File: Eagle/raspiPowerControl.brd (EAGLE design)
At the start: 100 x 80 mm, 10 parts, among them Q1 FDN360P, T1 BC847

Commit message: Update Eagle
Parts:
- added C3: 100n, rcl:C0805
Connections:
- net +5V: now also C3.2
- net GND: now also C3.1
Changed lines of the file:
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@@
 <attribute name="VALUE" x="-52.07" y="-50.8" size="1.27" layer="27"/>
+</element>
+<element name="C3" library="rcl" library_urn="urn:adsk.eagle:library:334" package="C0805" package3d_urn="urn:adsk.eagle:package:23617/2" value="100n" x="-57.15" y="-60.96" smashed="yes">
+<attribute name="NAME" x="-58.42" y="-59.69" size="1.27" layer="25"/>
+<attribute name="POPULARITY" value="88" x="-57.15" y="-60.96" size="1.778" layer="27" display="off"/>
+<attribute name="SPICEPREFIX" value="C" x="-57.15" y="-60.96" size="1.778" layer="27" display="off"/>
+<attribute name="VALUE" x="-58.42" y="-63.5" size="1.27" layer="27"/>
 </element>
 </elements>
@@
 <contactref element="SV1" pad="14"/>
 <contactref element="SV1" pad="9"/>
+<contactref element="C3" pad="1"/>
+<wire x1="-51.75" y1="-48.26" x2="-58.1" y2="-60.96" width="0" layer="19" extent="1-1"/>
 <wire x1="-50.8" y1="-38.1" x2="-51.75" y2="-48.26" width="0" layer="19" extent="1-1"/>
 <wire x1="-48.58" y1="-4.91" x2="-50.8" y2="-38.1" width="0" layer="19" extent="1-1"/>
-<wire x1="26.67" y1="26.67" x2="-48.58" y2="-4.91" width="0" layer="19" extent="1-1"/>
-<wire x1="38.1" y1="3.81" x2="26.67" y2="26.67" width="0" layer="19" extent="1-1"/>
+<wire x1="27.94" y1="3.81" x2="-48.58" y2="-4.91" width="0" layer="19" extent="1-1"/>
+<wire x1="33.02" y1="6.35" x2="27.94" y2="3.81" width="0" layer="19" extent="1-1"/>
 <wire x1="38.1" y1="3.81" x2="33.02" y2="6.35" width="0" layer="19" extent="1-1"/>
-<wire x1="27.94" y1="3.81" x2="33.02" y2="6.35" width="0" layer="19" extent="1-1"/>
+<wire x1="26.67" y1="26.67" x2="33.02" y2="6.35" width="0" layer="19" extent="1-1"/>
 </signal>
 <signal name="RP5V">
@@
 <contactref element="Q1" pad="2"/>
 <contactref element="+5V" pad="MP"/>
+<contactref element="C3" pad="2"/>
 <contactref element="LED1" pad="A"/>
+<wire x1="-50.952" y1="-43.18" x2="-56.2" y2="-60.96" width="0" layer="19" extent="1-1"/>
 <wire x1="-50.8" y1="-31.75" x2="-50.952" y2="-43.18" width="0" layer="19" extent="1-1"/>
 <wire x1="-49.85" y1="-24.13" x2="-50.8" y2="-31.75" width="0" layer="19" extent="1-1"/>
@@
 </signal>
 <signal name="PWR">
-<contactref element="LED1" pad="C"/>
 <contactref element="U$1" pad="5V"/>
 <contactref element="C1" pad="2"/>
+<contactref element="LED1" pad="C"/>
 <wire x1="-48.108" y1="-43.18" x2="-49.85" y2="-48.26" width="0" layer="19" extent="1-1"/>
 <wire x1="26.67" y1="29.21" x2="-48.108" y2="-43.18" width="0" layer="19" extent="1-1"/>

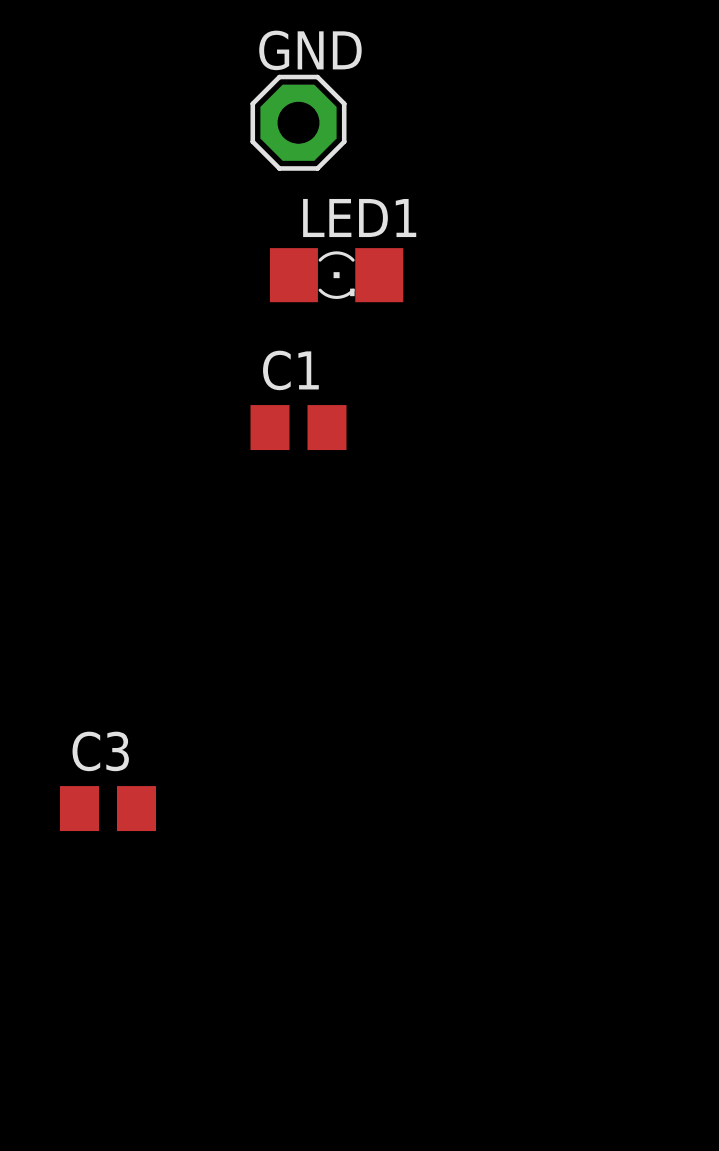
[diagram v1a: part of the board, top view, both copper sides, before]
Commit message: Add regulator to design
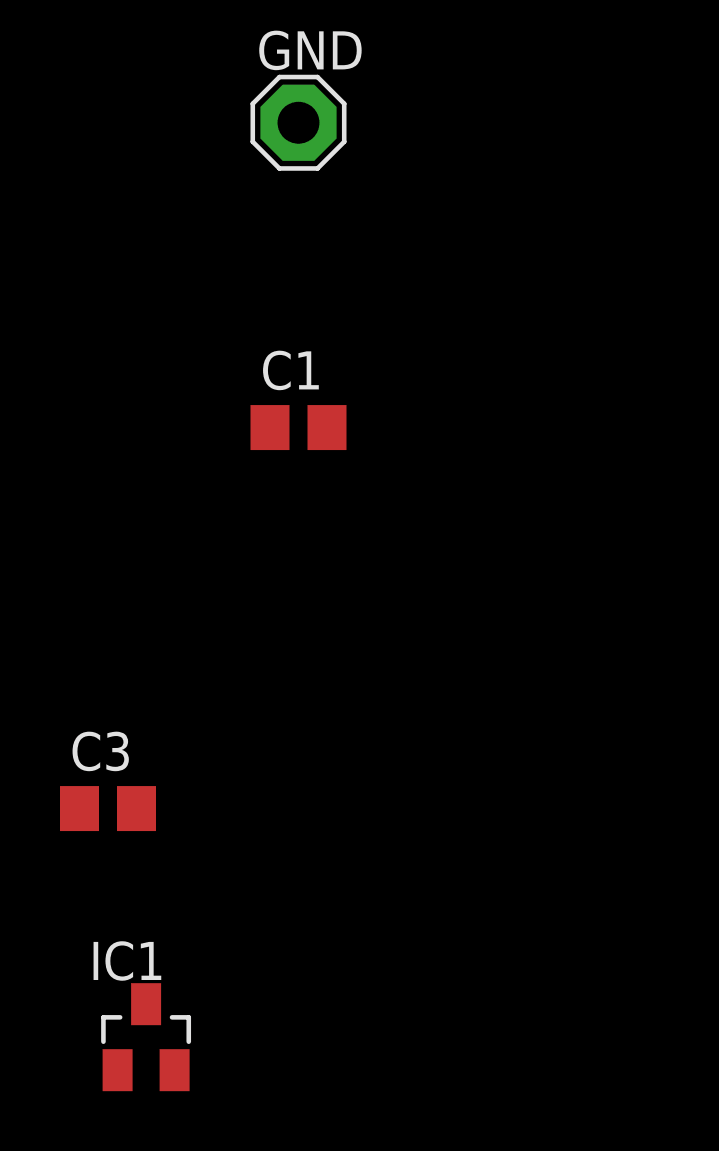
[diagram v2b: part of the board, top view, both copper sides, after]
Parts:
- removed LED1: red (1.7V), led:1206
- added IC1: MCP1702 3.3, linear:SOT23
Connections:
- removed net +5V: +5V.MP, C3.2, LED1.A, Q1.2, R2.2
- new net N$2: +5V.MP, C3.2, IC1.3, Q1.2, R2.2
- net GND: now also IC1.1
- net PWR: now also IC1.2; no longer LED1.C
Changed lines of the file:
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@@
 <attribute name="VALUE" x="-50.8" y="-37.719" size="0.0254" layer="27"/>
-</element>
-<element name="LED1" library="led" library_urn="urn:adsk.eagle:library:259" package="1206" package3d_urn="urn:adsk.eagle:package:15796/2" value="red (1.7V)" x="-49.53" y="-43.18" smashed="yes">
-<attribute name="NAME" x="-50.8" y="-41.91" size="1.27" layer="25"/>
-<attribute name="POPULARITY" value="20" x="-49.53" y="-43.18" size="1.778" layer="27" display="off"/>
-<attribute name="VALUE" x="-50.8" y="-45.72" size="1.27" layer="27"/>
 </element>
 <element name="C1" library="rcl" library_urn="urn:adsk.eagle:library:334" package="C0805" package3d_urn="urn:adsk.eagle:package:23617/2" value="1u" x="-50.8" y="-48.26" smashed="yes">
@@
 <attribute name="SPICEPREFIX" value="C" x="-57.15" y="-60.96" size="1.778" layer="27" display="off"/>
 <attribute name="VALUE" x="-58.42" y="-63.5" size="1.27" layer="27"/>
+</element>
+<element name="IC1" library="linear" library_urn="urn:adsk.eagle:library:262" package="SOT23" package3d_urn="urn:adsk.eagle:package:16489/2" value="MCP1702 3.3" x="-55.88" y="-68.58" smashed="yes">
+<attribute name="NAME" x="-57.785" y="-66.675" size="1.27" layer="25"/>
+<attribute name="POPULARITY" value="19" x="-55.88" y="-68.58" size="1.778" layer="27" display="off"/>
+<attribute name="VALUE" x="-57.785" y="-71.755" size="1.27" layer="27"/>
 </element>
 </elements>
@@
 <contactref element="SV1" pad="9"/>
 <contactref element="C3" pad="1"/>
+<contactref element="IC1" pad="1"/>
+<wire x1="-58.1" y1="-60.96" x2="-56.83" y2="-69.68" width="0" layer="19" extent="1-1"/>
 <wire x1="-51.75" y1="-48.26" x2="-58.1" y2="-60.96" width="0" layer="19" extent="1-1"/>
 <wire x1="-50.8" y1="-38.1" x2="-51.75" y2="-48.26" width="0" layer="19" extent="1-1"/>
@@
 <wire x1="43.18" y1="3.81" x2="-50.8" y2="-10.33" width="0" layer="19" extent="1-1"/>
 <wire x1="40.64" y1="3.81" x2="43.18" y2="3.81" width="0" layer="19" extent="1-1"/>
-</signal>
-<signal name="+5V">
-<contactref element="R2" pad="2"/>
-<contactref element="Q1" pad="2"/>
-<contactref element="+5V" pad="MP"/>
-<contactref element="C3" pad="2"/>
-<contactref element="LED1" pad="A"/>
-<wire x1="-50.952" y1="-43.18" x2="-56.2" y2="-60.96" width="0" layer="19" extent="1-1"/>
-<wire x1="-50.8" y1="-31.75" x2="-50.952" y2="-43.18" width="0" layer="19" extent="1-1"/>
-<wire x1="-49.85" y1="-24.13" x2="-50.8" y2="-31.75" width="0" layer="19" extent="1-1"/>
-<wire x1="-49.85" y1="-12.53" x2="-49.85" y2="-24.13" width="0" layer="19" extent="1-1"/>
 </signal>
 <signal name="N$3">
@@
 <contactref element="U$1" pad="5V"/>
 <contactref element="C1" pad="2"/>
-<contactref element="LED1" pad="C"/>
-<wire x1="-48.108" y1="-43.18" x2="-49.85" y2="-48.26" width="0" layer="19" extent="1-1"/>
-<wire x1="26.67" y1="29.21" x2="-48.108" y2="-43.18" width="0" layer="19" extent="1-1"/>
+<contactref element="IC1" pad="2"/>
+<wire x1="-49.85" y1="-48.26" x2="-54.93" y2="-69.68" width="0" layer="19" extent="1-1"/>
+<wire x1="26.67" y1="29.21" x2="-49.85" y2="-48.26" width="0" layer="19" extent="1-1"/>
 </signal>
 <signal name="SHUTDWN">
@@
 <wire x1="27.94" y1="6.35" x2="36.83" y2="16.51" width="0" layer="19" extent="1-1"/>
 </signal>
+<signal name="N$2">
+<contactref element="C3" pad="2"/>
+<contactref element="+5V" pad="MP"/>
+<contactref element="R2" pad="2"/>
+<contactref element="Q1" pad="2"/>
+<contactref element="IC1" pad="3"/>
+<wire x1="-56.2" y1="-60.96" x2="-55.88" y2="-67.48" width="0" layer="19" extent="1-1"/>
+<wire x1="-50.8" y1="-31.75" x2="-56.2" y2="-60.96" width="0" layer="19" extent="1-1"/>
+<wire x1="-49.85" y1="-24.13" x2="-50.8" y2="-31.75" width="0" layer="19" extent="1-1"/>
+<wire x1="-49.85" y1="-12.53" x2="-49.85" y2="-24.13" width="0" layer="19" extent="1-1"/>
+</signal>
 </signals>

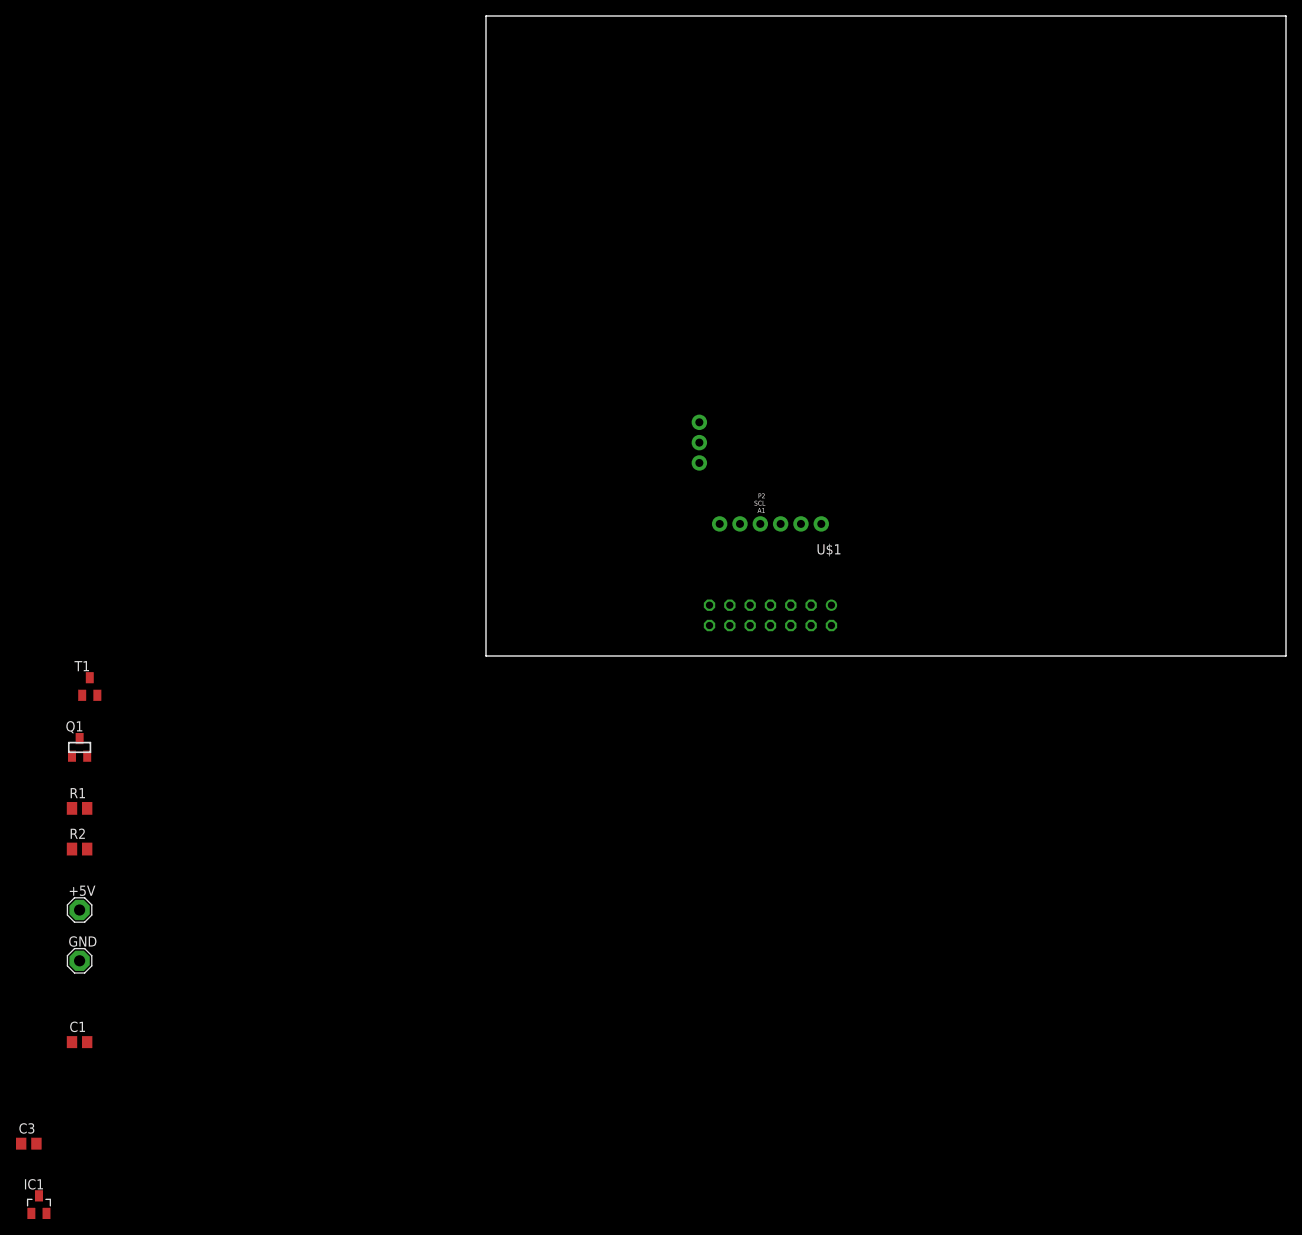
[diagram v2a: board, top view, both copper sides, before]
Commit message: Add DC/DC converter to design
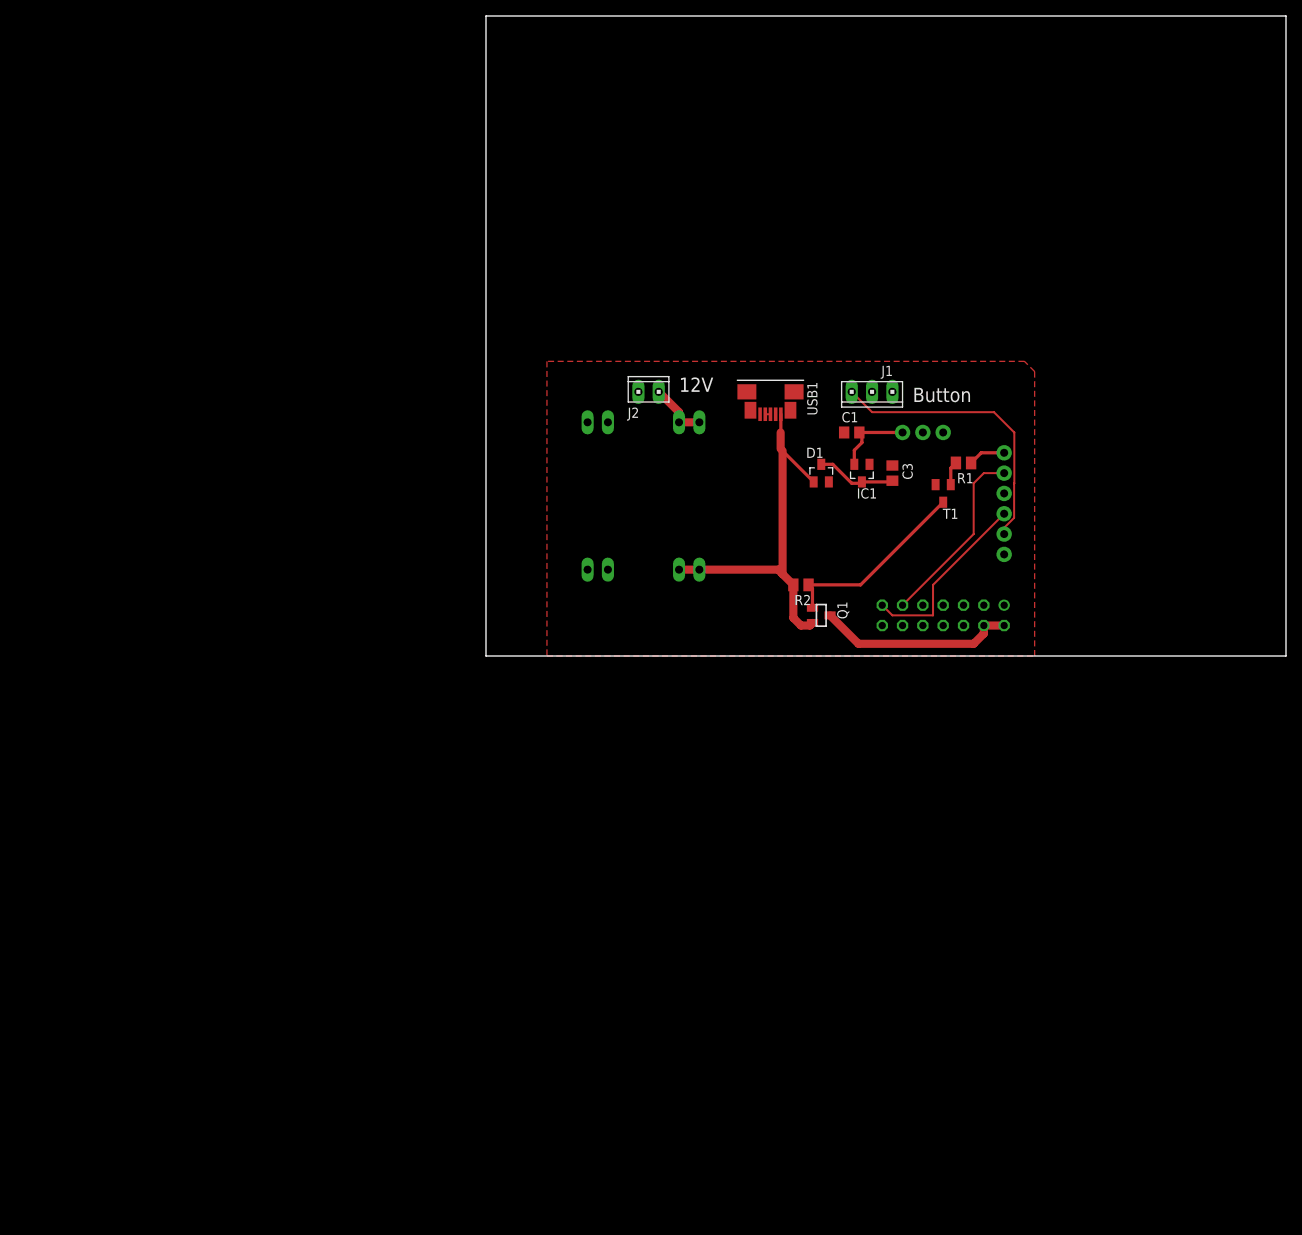
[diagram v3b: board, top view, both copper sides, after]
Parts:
- removed +5V, GND: SE14, solpad:SE14
- removed U$1: DIGISPARK, raspiPowerControl:DIGISPARK
- added ATTINY85: DIGISPARK, raspiPowerControl:DIGISPARK
- added D1: BAS40, diode:SOT23
- added J1: (no value), con-amp:10X03MTA
- added J2: (no value), con-amp:10X02MTA
- added MP1584: DCDC-MINI, raspiPowerControl:DCDC-MINI
- added USB1: MOLEX-47346-0001, usb_con-update:MOLEX-47364-0001
- IC1: value MCP1702 3.3 -> MCP1702/3 3.3
- moved IC1 137.6 mm to (47.0, 22.9), turned to 180 degrees
- moved C3 136.7 mm to (50.8, 22.9), turned to 270 degrees
- moved C1 123.0 mm to (45.7, 27.9)
- moved R1 118.6 mm to (59.7, 24.1), turned to 180 degrees
- moved T1 109.4 mm to (57.1, 20.3), turned to 180 degrees
- moved R2 96.0 mm to (39.4, 8.89), turned to 180 degrees
- moved Q1 94.2 mm to (41.9, 5.08), turned to 270 degrees
- moved SV1 21.6 mm to (57.1, 5.08)
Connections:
- new net +12V: J2.1, MP1584.3, MP1584.4
- new net +5V: D1.1, MP1584.5, MP1584.6, Q1.2, R2.2, USB1.1
- new net N$1: C3.2, D1.3, IC1.3
- new net N$6: ATTINY85.P4, J1.1
- net GND: now also ATTINY85.GND, J1.2, J2.2, MP1584.1, MP1584.2, MP1584.7, MP1584.8, USB1.5; no longer GND.MP, U$1.GND
- net N$2: now also USB1.3, USB1.4; no longer +5V.MP, C3.2, IC1.3, Q1.2, R2.2
- net N$5: now also ATTINY85.P0; no longer U$1.P0
- net PWR: now also ATTINY85.5V, J1.3; no longer U$1.5V
- net RPDWN: now also ATTINY85.P3; no longer U$1.P3
- net SHUTDWN: now also ATTINY85.P1; no longer U$1.P1
- net VIN: now also ATTINY85.VIN; no longer U$1.VIN
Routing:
- net +5V: track 0.00 -> 47.7 mm
- net N$6: track 0.00 -> 35.7 mm
- net RP5V: track 0.00 -> 24.8 mm
- net N$3: track 0.00 -> 24.2 mm
- net RPDWN: track 0.00 -> 23.3 mm
- net SHUTDWN: track 0.00 -> 23.3 mm
- net N$1: track 0.00 -> 10.0 mm
- net PWR: track 0.00 -> 9.91 mm
- net +12V: track 0.00 -> 7.40 mm
- net N$5: track 0.00 -> 4.66 mm
- net N$4: track 0.00 -> 2.98 mm
- net N$2: track 0.00 -> 0.65 mm
- added copper zone on layer 1, net GND
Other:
- board text added: "12V"
- board text added: "Button"
